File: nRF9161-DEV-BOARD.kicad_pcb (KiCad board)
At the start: 4 copper layers, 120 x 80 mm, 102 parts, among them J1 VIN_3V0-5V5, J10 SPI0, J11 I2C0, J12 GPIO_P0.00-15, J13 GPIO_P0.16-31, J14 RFFE_MAGPIO, J15 COEX, J16 I2S, J17 PDM, J18 ADC_AIN0-7, J2 U.FL_LTE_NR+, J3 SWF_LTE, J5 U.FL_GNSS, J6 SWF_GNSS, J7 nanoSIM_4FF, J8 SWD_10pin, J9 UART0, SW1 DISABLE, SW2 RESET, SW3 USER, U1 NRF9161-LACA-R7, U2 TLV73330PDBV, U4 TPD3F303DPV

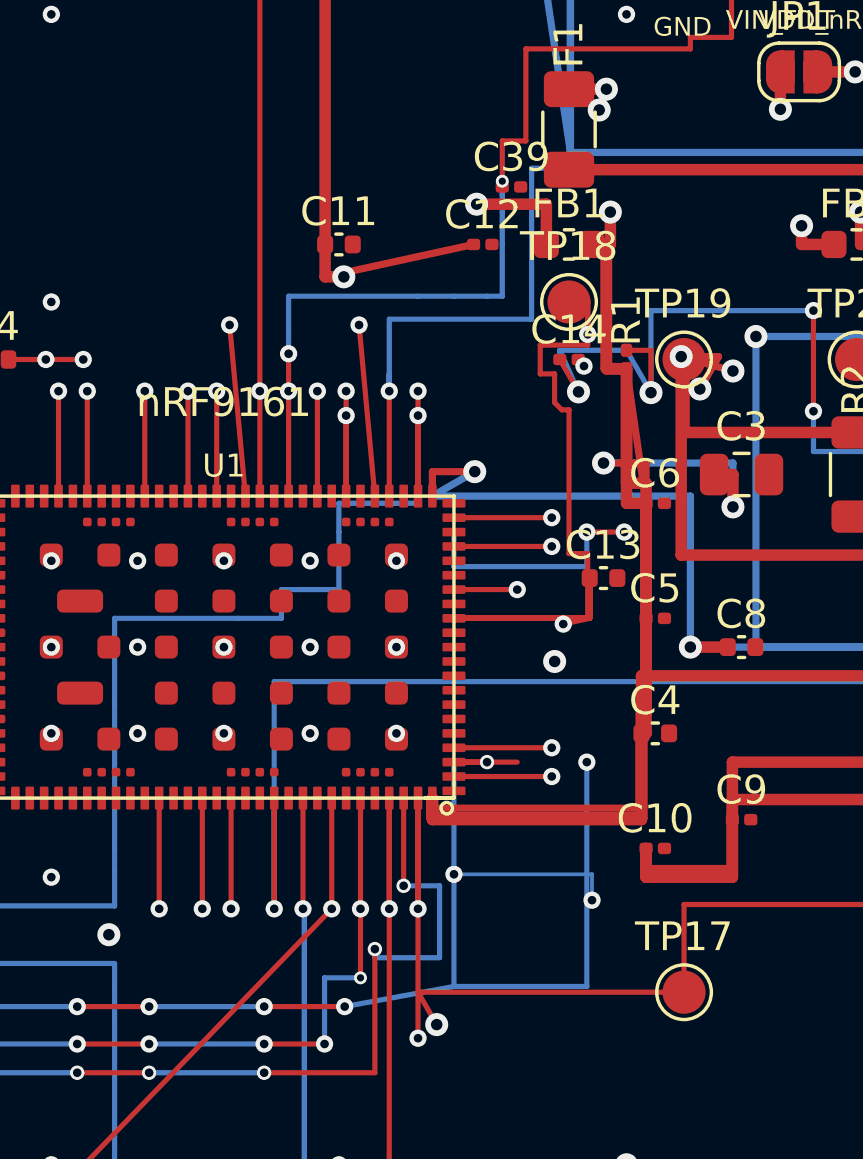
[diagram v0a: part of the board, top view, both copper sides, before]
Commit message: Schematic: GNSS COEX0 bias switch, 3.3V VDD_GPIO, DNP RF shunts
- Add U3 TPS22919DCKR on 04_GNSS (COEX0-gated bias); FB5 0402
- Swap U2 to TLV73333 (3.3 V VDD_GPIO); DNP Class-C shunt caps
- Quarantine leftover schematics/; remove stale ERC rpt
- Add PM/DFM/RF/schematic/layout review docs under docs/
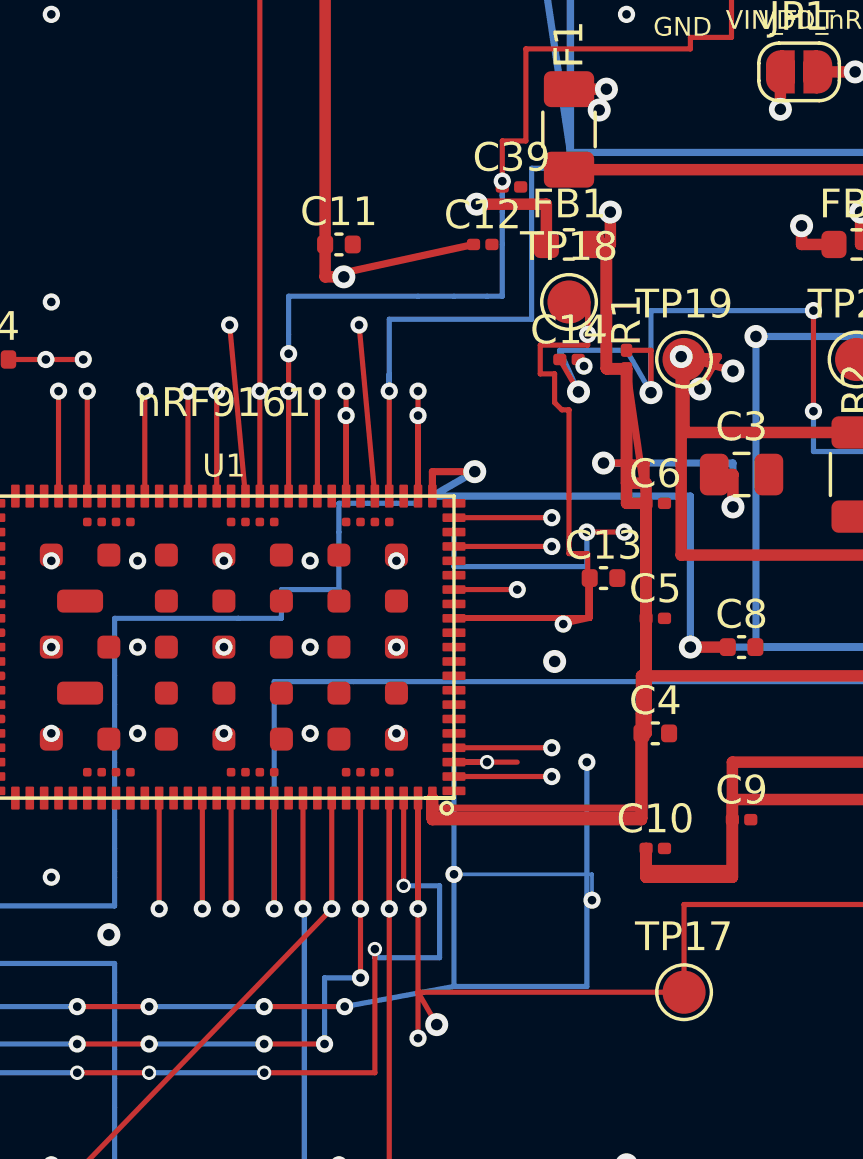
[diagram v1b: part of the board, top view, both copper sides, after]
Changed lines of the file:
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@@
 	(via
 		(at 40.75 43.5)
-		(size 0.45)
-		(drill 0.25)
+		(size 0.60)
+		(drill 0.30)
 		(layers "F.Cu" "B.Cu")
 		(net 50)
@@
 	(via
 		(at 45.68 15.8)
-		(size 0.45)
-		(drill 0.25)
-		(layers "F.Cu" "B.Cu")
-		(net 55)
+		(size 0.60)
+		(drill 0.30)
+		(layers "F.Cu" "B.Cu")
+		(net 55)

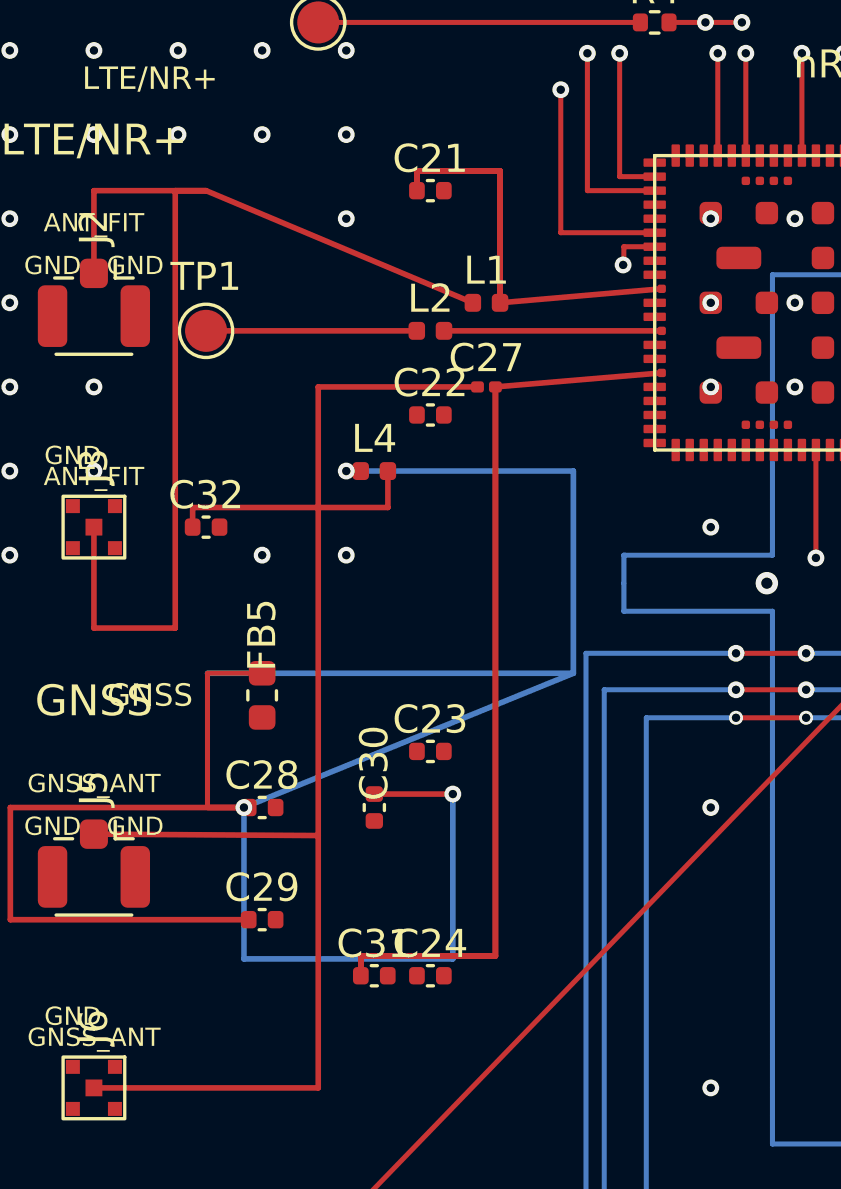
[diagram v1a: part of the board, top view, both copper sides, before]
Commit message: PCB pass30: place U3 GNSS bias switch, close bias nets
Partial connect pass: U3 TPS22919 east of RF keepout, FB5 0402,
GNSS bias path closed; U3 VIN/COEX0 and Class F still open.
Clearance cleaned; unconnected ~80. No Gerbers.
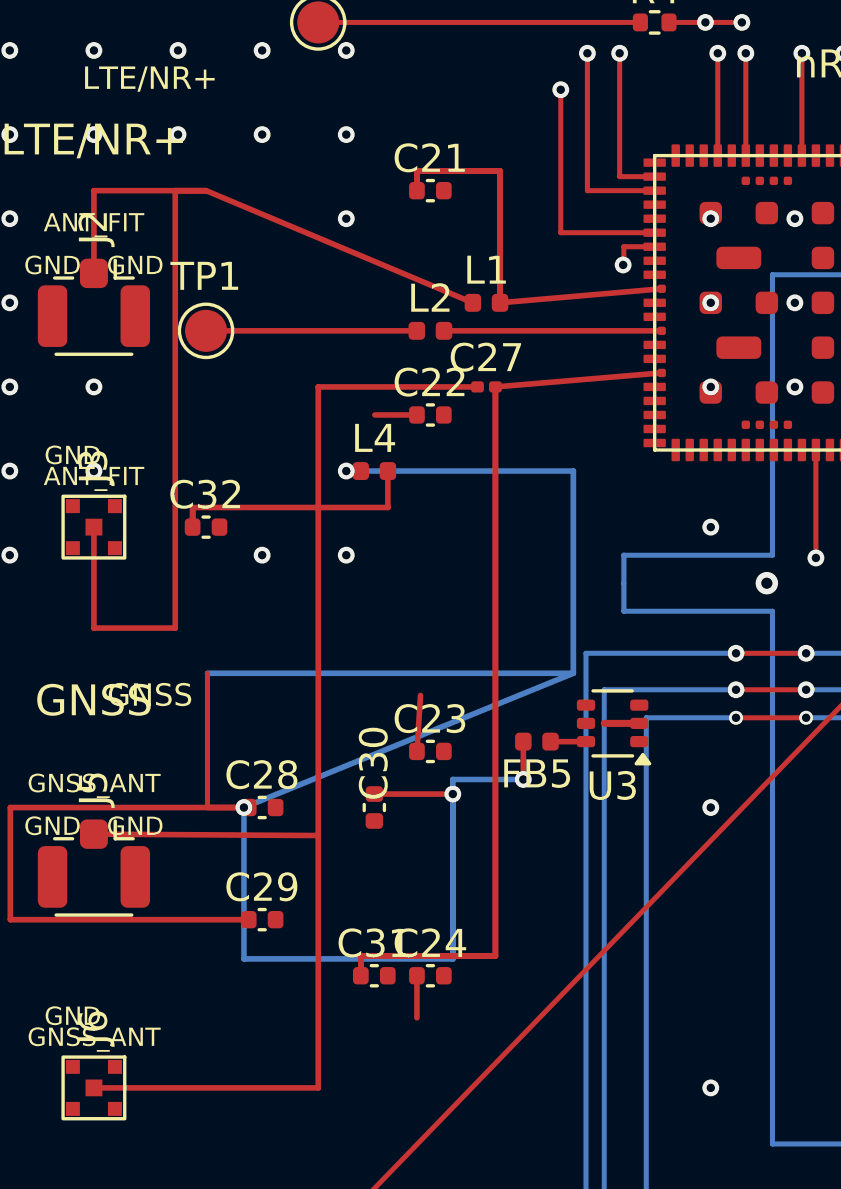
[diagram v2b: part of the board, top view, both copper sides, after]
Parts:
- added U3: TPS22919DCKR, SOT-363_SC-70-6, F.Cu at (26.5, 47.0)
- FB5: footprint Inductor_SMD:L_0603_1608Metric -> L_0402_1005Metric
- moved FB5 9.94 mm to (23.8, 47.6), turned to 180 degrees
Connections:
- FB5 pad 1: VDD_GPIO -> GNSS_VBIAS_SRC
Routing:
- net GNSS_VBIAS: track 114.6 -> 122.9 mm, vias 3 -> 4
- net AUX: track 7.77 -> 9.77 mm
- net AUX_FIT: track 7.52 -> 9.02 mm
- net ANT_FIT: track 40.5 -> 42.0 mm
- net GNSS_VBIAS_SRC: track 0.00 -> 1.27 mm
- net GND: track 0.00 -> 1.25 mm
- net GPS: track 57.6 -> 58.3 mm
- net GNSS_ANT: track 55.6 -> 56.3 mm
- net ANT: track 22.5 -> 23.2 mm

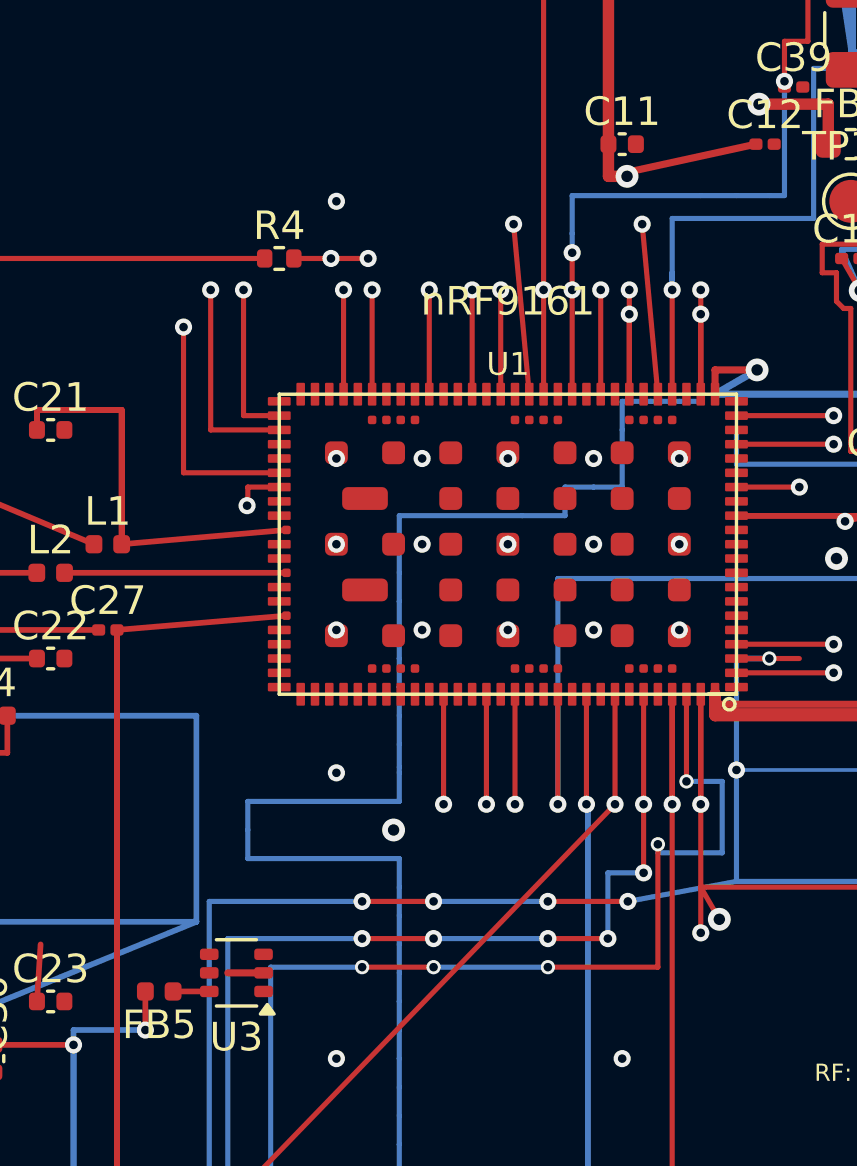
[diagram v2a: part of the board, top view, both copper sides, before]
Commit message: PCB pass30c: sync U3 nets, close VDD_GPIO/COEX0; unconnected 80→78
Commit layout board, review notes, PASS30C summary and after-DRC. Ignore *.kicad_net exports. Exclude .mcp-backups.
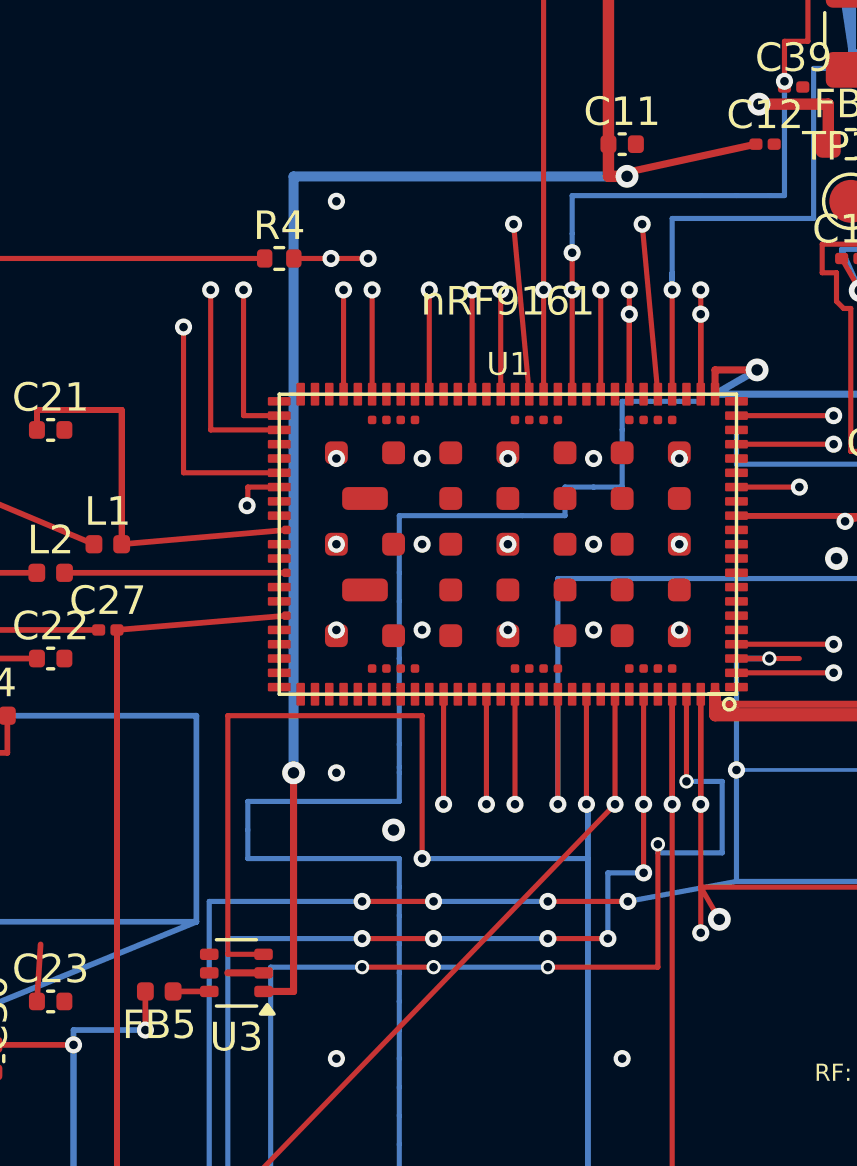
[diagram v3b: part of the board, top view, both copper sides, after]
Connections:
- U3 pad 4: (no net) -> unconnected-(U3-NC-Pad4)
- U3 pad 5: (no net) -> unconnected-(U3-QOD-Pad5)
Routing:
- net VDD_GPIO: track 342.8 -> 384.0 mm, vias 9 -> 10
- net COEX0: track 188.3 -> 215.5 mm, vias 3 -> 4
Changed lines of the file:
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@@
 	(net 79 "VIN_F")
 	(net 80 "GNSS_VBIAS_SRC")
+	(net 81 "unconnected-(U3-NC-Pad4)")
+	(net 82 "unconnected-(U3-QOD-Pad5)")
 	(footprint "Capacitor_SMD:C_0201_0603Metric"
 		(layer "F.Cu")
@@
 			(layers "F.Cu" "F.Mask" "F.Paste")
 			(roundrect_rratio 0.25)
+			(net 81 "unconnected-(U3-NC-Pad4)")
 		)
 		(pad "5" smd roundrect
@@
 			(layers "F.Cu" "F.Mask" "F.Paste")
 			(roundrect_rratio 0.25)
+			(net 82 "unconnected-(U3-QOD-Pad5)")
 		)
 		(pad "6" smd roundrect
@@
 	)
 	(segment
+		(start 27.45 47.65)
+		(end 28.5 47.65)
+		(width 0.25)
+		(layer "F.Cu")
+		(net 22)
+	)
+	(segment
 		(start 104 67.08)
 		(end 105.1 67.08)
@@
 	)
 	(segment
+		(start 28.5 47.65)
+		(end 28.5 40)
+		(width 0.25)
+		(layer "F.Cu")
+		(net 22)
+	)
+	(segment
 		(start 48.05 3.46)
 		(end 46.349999 3.46)
@@
 	)
 	(via
+		(at 28.5 40)
+		(size 0.8)
+		(drill 0.4)
+		(layers "F.Cu" "B.Cu")
+		(net 22)
+	)
+	(via
 		(at 70 8)
 		(size 0.8)
@@
 	)
 	(segment
+		(start 28.5 19.13)
+		(end 40.17 19.13)
+		(width 0.35)
+		(layer "B.Cu")
+		(net 22)
+	)
+	(segment
 		(start 46.64 76)
 		(end 49.18 76)
@@
 	)
 	(segment
+		(start 28.5 40)
+		(end 28.5 19.13)
+		(width 0.35)
+		(layer "B.Cu")
+		(net 22)
+	)
+	(segment
 		(start 110.6 38.8)
 		(end 116 38.8)
@@
 	)
 	(segment
+		(start 26.2 38)
+		(end 33 38)
+		(width 0.18)
+		(layer "F.Cu")
+		(net 34)
+	)
+	(segment
+		(start 33 38)
+		(end 33 43)
+		(width 0.18)
+		(layer "F.Cu")
+		(net 34)
+	)
+	(segment
 		(start 29.81 22)
 		(end 31.11 22)
@@
 	)
 	(segment
+		(start 26.2 46.35)
+		(end 26.2 38)
+		(width 0.18)
+		(layer "F.Cu")
+		(net 34)
+	)
+	(segment
 		(start 38.75 37.25)
 		(end 38.75 41.1)
@@
 		(net 34)
 	)
+	(segment
+		(start 27.45 46.35)
+		(end 26.2 46.35)
+		(width 0.18)
+		(layer "F.Cu")
+		(net 34)
+	)
+	(via
+		(at 33 43)
+		(size 0.6)
+		(drill 0.3)
+		(layers "F.Cu" "B.Cu")
+		(net 34)
+	)
 	(via
 		(at 29.81 22)
@@
 		(width 0.18)
 		(layer "B.Cu")
+		(net 34)
+	)
+	(segment
+		(start 33 43)
+		(end 38.8 43)
+		(width 0.18)
+		(layer "B.Cu")
